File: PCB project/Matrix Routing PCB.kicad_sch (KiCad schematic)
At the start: 14 parts, among them J1 Connector 1x6, J2 JST_PH_S4B-PH-SM4-TB_1x04-1MP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, J3 ESQ-105-11-T-D, J4 TSM-102-01-L-DH-A, J5 USB-A-S-X-X-SM2-R, U1 FT232RL

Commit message: V1 prepare for generating the manufacturing files
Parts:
- C1, C3: value C -> 100nF; Digikey PN (none) -> 399-C0603C104K4RACTUCT-ND; MANUFACTURER (none) -> Yageo Group; MPN (none) -> C0603C104K4RACTU; RS PN (none) -> 264-4630
- C2: value C -> 10nF; Digikey PN (none) -> 399-C0603C103K5RACTUCT-ND; MANUFACTURER (none) -> Yageo Group; MPN (none) -> C0603C103K5RACTU; RS PN (none) -> 264-4595
- C4: value C -> 4.7uF; Digikey PN (none) -> 490-16337-1-ND; MANUFACTURER (none) -> Murata; MPN (none) -> GRM188C71C475KE21D; RS PN (none) -> 247-8044
- J1: value Connector 1x6 -> 53261-0471; Digikey PN (none) -> WM7622CT-ND; MANUFACTURER (none) -> Molex; RS PN 688-1366 -> 542-7113
- J2: value JST_PH_S4B-PH-SM4-TB_1x04-1MP_P2.00mm_Horizontal -> JST_PH_S4B-PH-SM4-TB; Digikey PN (none) -> 455-S4B-PH-SM4-TBCT-ND; MANUFACTURER (none) -> JST
- J3: value ESQ-105-11-T-D -> ESQ-105-12-T-D; Digikey PN (none) -> SAM15563-ND; MANUFACTURER (none) -> Samtec; MPN ESQ-105-23-T-D -> ESQ-105-12-T-D; RS PN 197-6628 -> 208-1157
- J4: Digikey PN (none) -> SAM15344-ND; MPN (none) -> TSM-102-01-L-DH-A; RS PN (none) -> 765-6423
- J5: value USB-A-S-X-X-SM2-R -> USB-A-S-F-B-SM2-R-TR; Digikey PN (none) -> 612-USB-A-S-F-B-SM2-R-TRCT-ND; RS PN (none) -> 227-2031
- U1: Digikey PN (none) -> 768-1306-ND; MANUFACTURER (none) -> FTDI; MPN (none) -> FT232RL; RS PN (none) -> 406-580

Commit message: Commit after review
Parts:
- J3: value ESQ-105-12-T-D -> ESQ-105-34-T-D; Digikey PN SAM15563-ND -> ESQ-105-33-T-D-ND; MPN ESQ-105-12-T-D -> ESQ-105-33-T-D; RS PN 208-1157 -> 208-1163
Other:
- note added: "The pins are too long and they need to be cut or they will collide with the metal work."
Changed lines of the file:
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@@
 	)
 	(rectangle
-		(start 77.47 46.99)
-		(end 158.75 90.17)
+		(start 73.66 46.99)
+		(end 161.29 90.17)
 		(stroke
 			(width 0)
@@
 		(exclude_from_sim no)
 		(at 171.45 45.72 0)
+		(effects
+			(font
+				(size 1.27 1.27)
+			)
+		)
+	)
+	(text "The pins are too long and they need to be cut or they will collide with the metal work."
+		(exclude_from_sim no)
+		(at 118.11 85.09 0)
 		(effects
 			(font
@@
 			)
 		)
-		(property "Value" "ESQ-105-12-T-D"
+		(property "Value" "ESQ-105-34-T-D"
 			(at 113.03 78.74 0)
 			(show_name no)
@@
 			)
 		)
-		(property "Digikey PN" "SAM15563-ND"
+		(property "Digikey PN" "ESQ-105-33-T-D-ND"
 			(at 110.49 71.12 0)
 			(hide yes)
@@
 			)
 		)
-		(property "MPN" "ESQ-105-12-T-D"
+		(property "MPN" "ESQ-105-33-T-D"
 			(at 110.49 71.12 0)
 			(hide yes)
@@
 			)
 		)
-		(property "RS PN" " 208-1157"
+		(property "RS PN" "208-1163"
 			(at 110.49 71.12 0)
 			(hide yes)

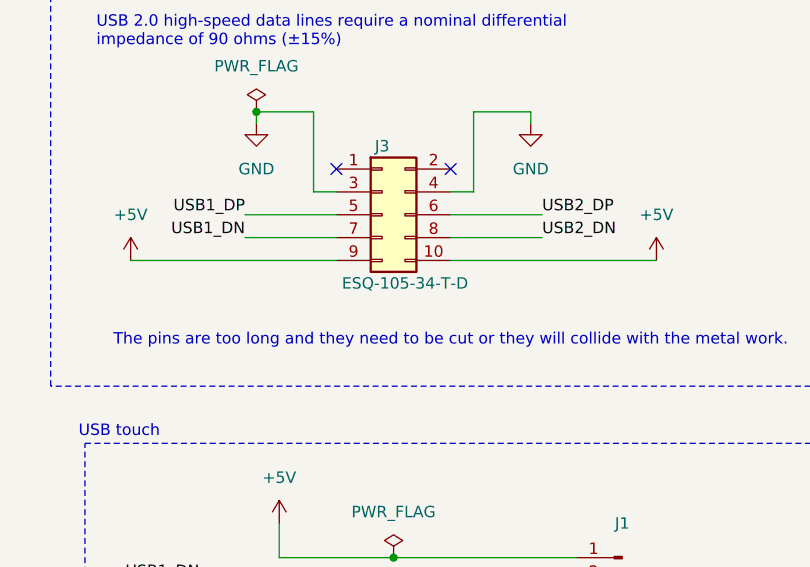
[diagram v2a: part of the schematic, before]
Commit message: Change the ESQ-105-33-T-D to ESQ-105-23-T-D
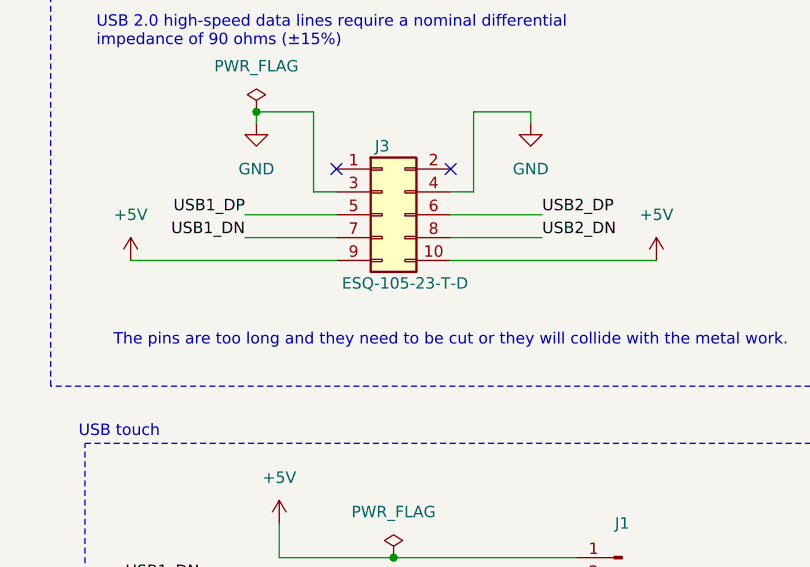
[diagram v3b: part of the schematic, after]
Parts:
- J3: value ESQ-105-34-T-D -> ESQ-105-23-T-D; Digikey PN ESQ-105-33-T-D-ND -> ESQ-105-23-T-D-ND; RS PN 208-1163 -> TBD
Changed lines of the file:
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@@
 			)
 		)
-		(property "Value" "ESQ-105-34-T-D"
+		(property "Value" "ESQ-105-23-T-D"
 			(at 113.03 78.74 0)
 			(show_name no)
@@
 			)
 		)
-		(property "Description" "PC/104 Connectors Elevated Socket Strip"
+		(property "Description" "Generic connector, double row, 02x05, odd/even pin numbering scheme (row 1 odd numbers, row 2 even numbers), script generated (kicad-library-utils/schlib/autogen/connector/)"
 			(at 110.49 71.12 0)
 			(hide yes)
@@
 			)
 		)
-		(property "Digikey PN" "ESQ-105-33-T-D-ND"
+		(property "Digikey PN" "ESQ-105-23-T-D-ND"
 			(at 110.49 71.12 0)
 			(hide yes)
@@
 			)
 		)
-		(property "RS PN" "208-1163"
+		(property "RS PN" "TBD"
 			(at 110.49 71.12 0)
 			(hide yes)
